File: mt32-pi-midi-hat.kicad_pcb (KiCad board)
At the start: 2 copper layers, 64.3 x 56 mm, 22 parts, among them J1 MIDI IN, J2 OLED, J3 OLED, J4 DAC BOARD, J5 DAC BOARD, J6 CONTROL_PINS, J7 POST, J8 POST, SW1 BUTTON_1, SW2 BUTTON_2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

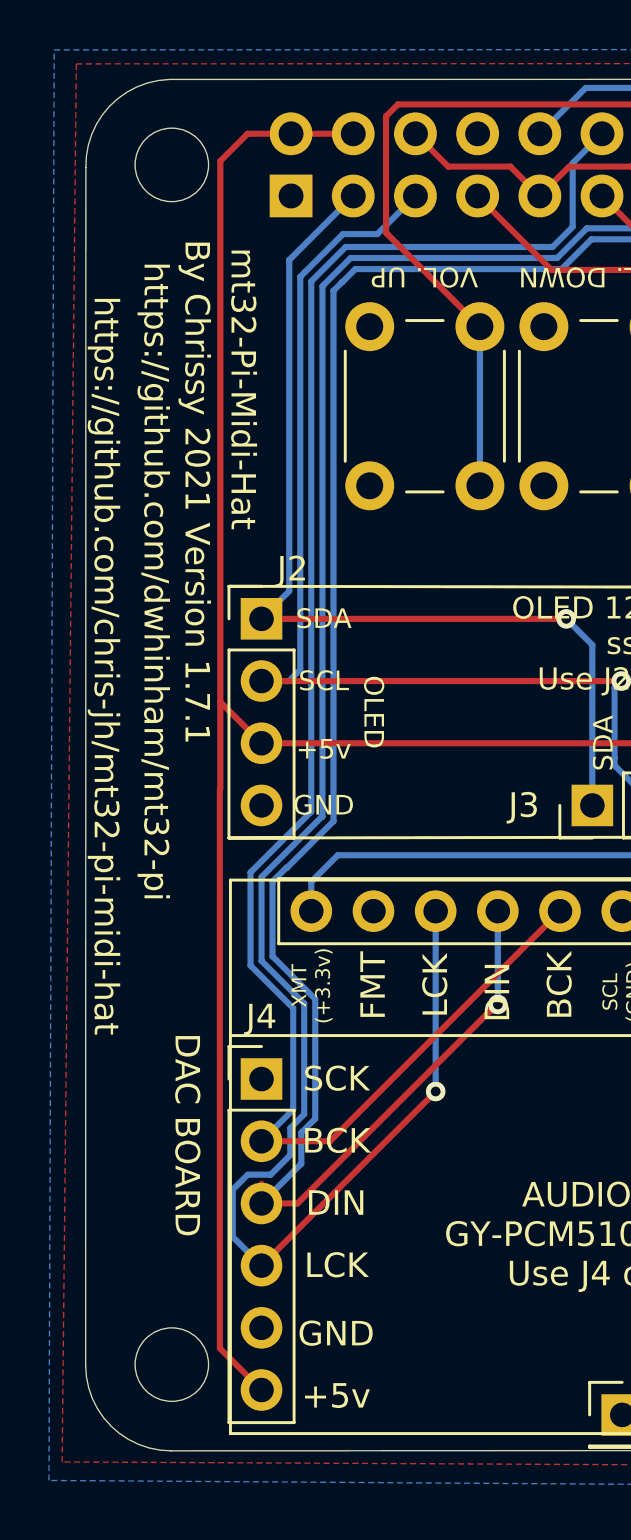
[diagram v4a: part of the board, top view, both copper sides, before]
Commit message: Version 1.7.2
moved a trace too near the mounting screw hole
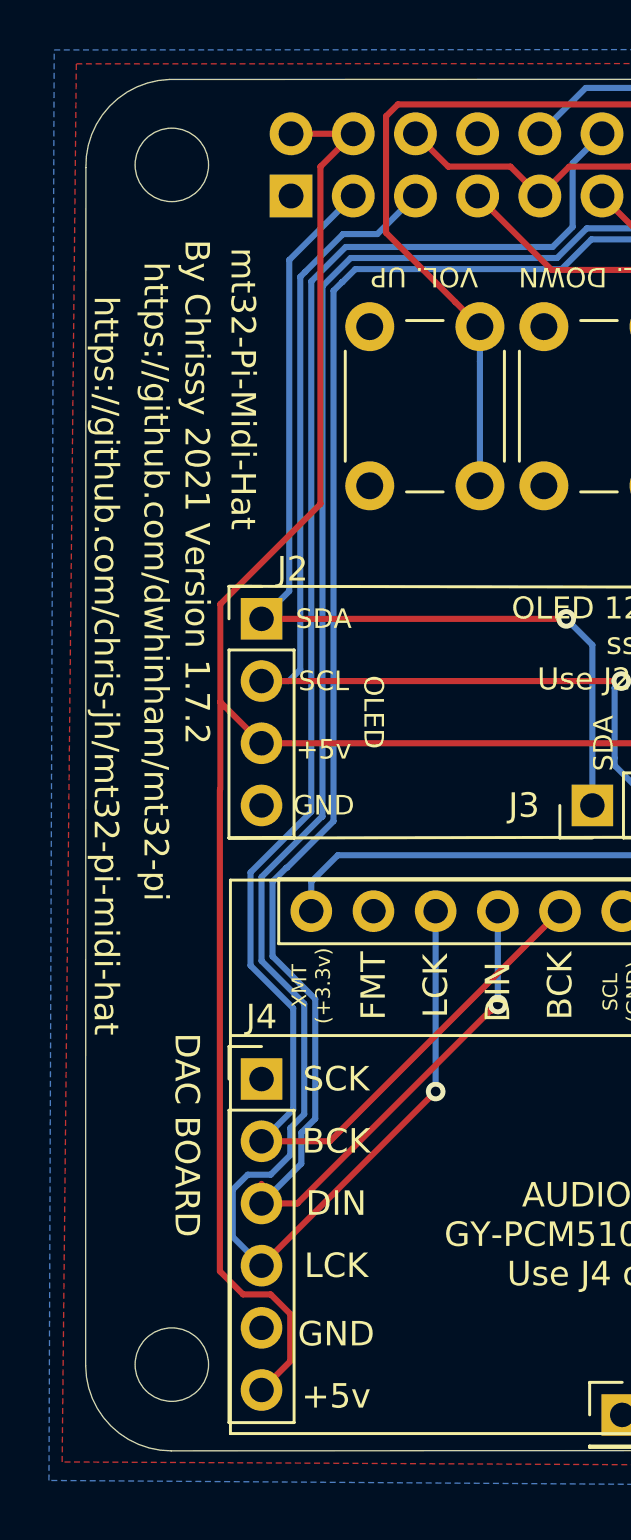
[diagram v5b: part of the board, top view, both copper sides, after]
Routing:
- net +5V: track 93.5 -> 95.2 mm
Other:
- board text added: "By Chrissy 2021 Version 1.7.2"
